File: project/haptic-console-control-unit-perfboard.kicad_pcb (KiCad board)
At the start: 2 copper layers, 90 x 144 mm, 239 parts, among them J1 JST-XH-5, J2 JST-XH-5

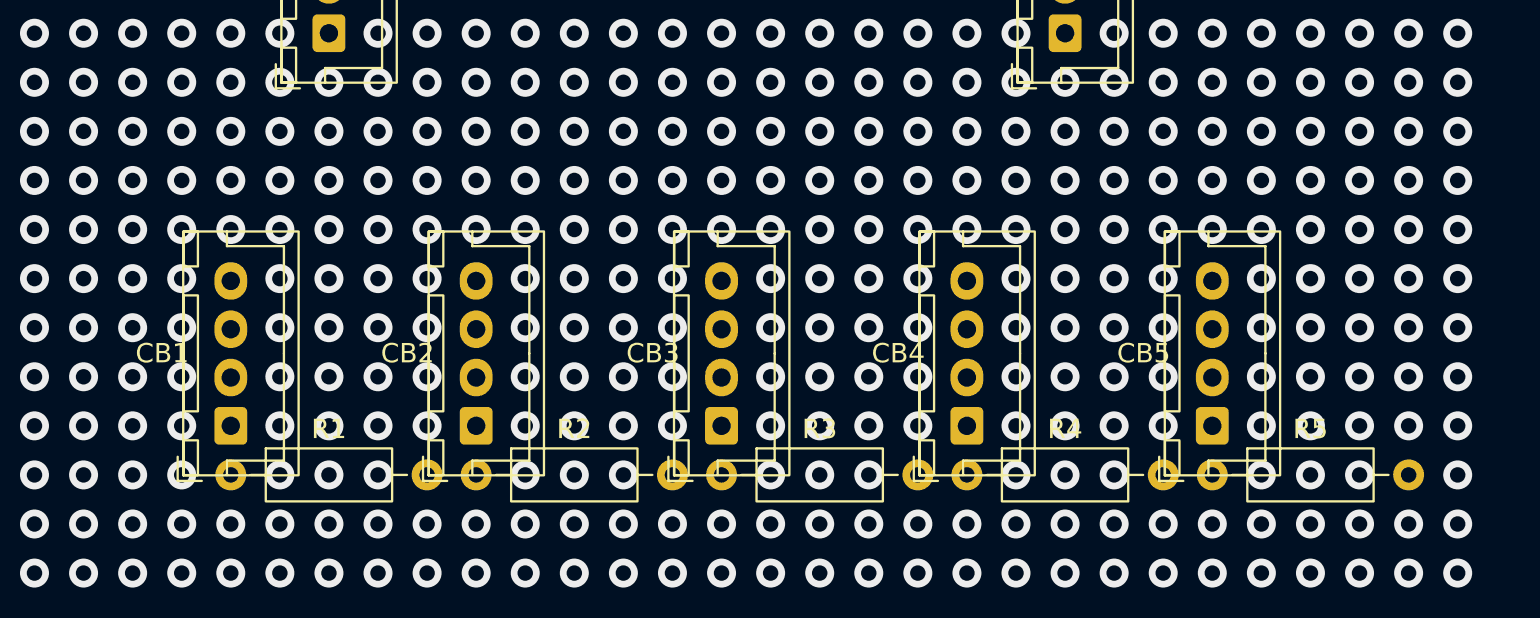
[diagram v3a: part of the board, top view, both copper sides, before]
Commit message: Resync every KiCad artifact to the current pin map (LED4 frozen on D13)
R4's LED jumper was re-landed from R29 (D16 = J1 pin 4, already soldered) to
O29 (D13), clearing the hardware conflict flagged last session. LED4 joins the
frozen set, which now holds 18 already-soldered conductors: B1-B8, J1/J2, LED4,
LED5. Freezing it costs nothing -- the solver had already chosen D13 -- so the
map stays at 1356.3 mm total Manhattan run, 61.0 mm longest wire.

- Schematic: 44 net labels renamed to their GPIO names (D<n>) via delete +
  re-add at identical coordinates. 2244 lines, 141 labels, ERC 0/0, 63 nets,
  all 40 signals verified on their intended U1 pin from the netlist libparts.
- Manufactured board: re-netted from a fresh netlist dump and re-routed via
  DSN -> Freerouting -> SES. 654 segments, 35 vias, DRC 0 violations /
  0 unconnected pads. Needed -mp 40; -mp 6 exited clean at 991.13 with one
  net still unrouted.
- Perfboard: R1-R5 moved upright beside their own CB in KiCad (they had only
  been patched into board_model.json before), 223 back-side jumper legs across
  6 tiers, 0 emit violations, 0 same-tier conflicts. Pristine DRC baseline is
  now 451 (was 478) -- moving the resistors off row 48 removed 27 violations --
  and the wired board's violation multiset is identical to it.
- Gerbers re-exported and re-zipped; all six renders regenerated, with zero
  wire overflow in all six colours confirmed by pixel measurement.
- Docs: wiring-guide.html regenerated (107 connections, 3006 mm, 157 pads /
  223 wires), panel-wiring-guide.html and README.md updated to match.

Co-Authored-By: Claude Opus 5 <noreply@anthropic.com>
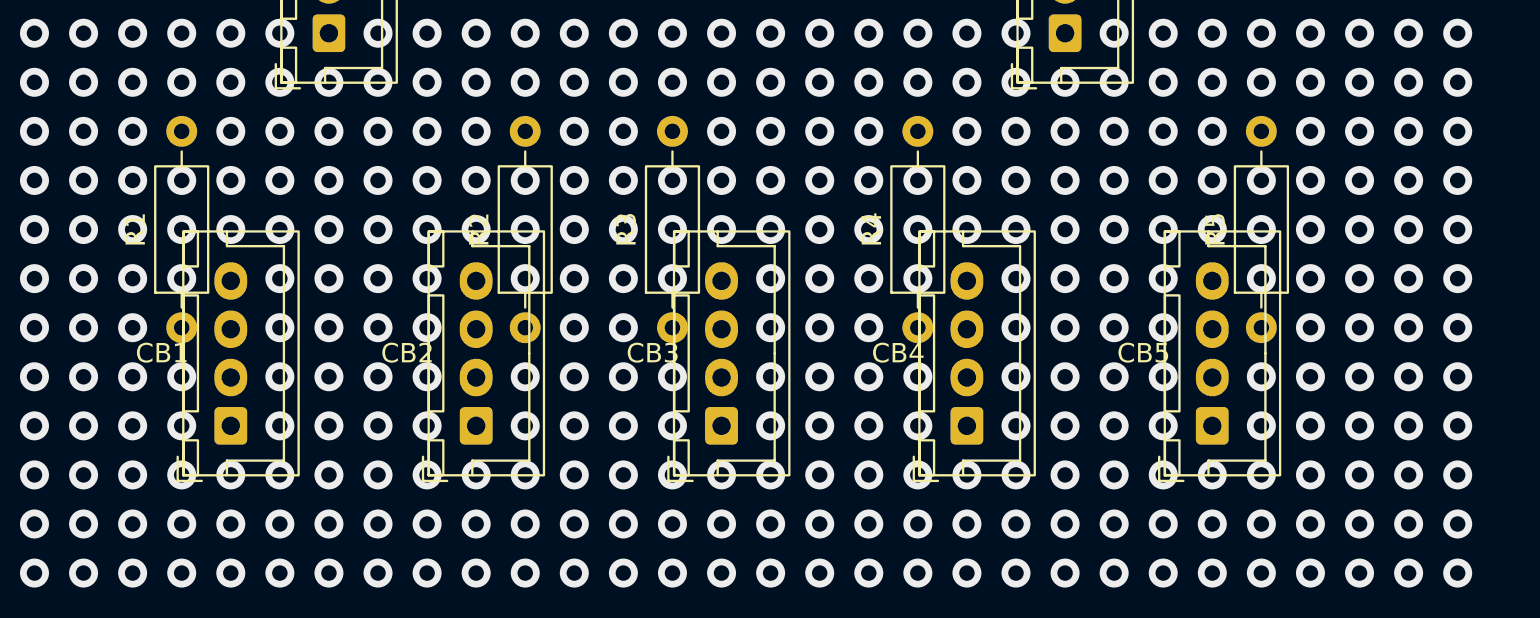
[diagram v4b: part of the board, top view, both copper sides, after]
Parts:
- added W204: D34 CB5.1->J_TEENSY_B.23, , B.Cu at (68.6, 92.8)
- added W205: D33 NP1.1->J_TEENSY_B.24, , B.Cu at (78.7, 94.0)
- added W206: D33 NP1.1->J_TEENSY_B.24, , B.Cu at (54.6, 111.8)
- added W207: D33 NP1.1->J_TEENSY_B.24, , B.Cu at (30.5, 71.2)
- added W208: D33 NP1.1->J_TEENSY_B.24, , B.Cu at (30.5, 108.0)
- added W209: D33 NP1.1->J_TEENSY_B.24, , B.Cu at (31.8, 104.1)
- added W210: D33 NP1.1->J_TEENSY_B.24, , B.Cu at (33.0, 88.9)
- added W211: D33 NP1.1->J_TEENSY_B.24, , B.Cu at (31.8, 73.7)
- added W212: D33 NP1.1->J_TEENSY_B.24, , B.Cu at (50.8, 68.7)
- added W213: D33 NP1.1->J_TEENSY_B.24, , B.Cu at (71.1, 71.2)
- added W214: LED_ARM CB1.3->R1.1, , B.Cu at (17.8, 114.3)
- added W215: LED_ARM CB1.3->R1.1, , B.Cu at (16.5, 114.3)
- added W216: LED_EN CB2.3->R2.1, , B.Cu at (30.5, 114.3)
- added W217: LED_EN CB2.3->R2.1, , B.Cu at (31.8, 114.3)
- added W218: LED_SFT CB3.3->R3.1, , B.Cu at (43.2, 114.3)
- added W219: LED_SFT CB3.3->R3.1, , B.Cu at (41.9, 114.3)
- added W220: LED_CONF CB4.3->R4.1, , B.Cu at (55.9, 114.3)
- added W221: LED_CONF CB4.3->R4.1, , B.Cu at (54.6, 114.3)
- added W222: LED_ALT CB5.3->R5.1, , B.Cu at (68.6, 114.3)
- added W223: LED_ALT CB5.3->R5.1, , B.Cu at (69.8, 114.3)
- W100, W101, W102: value D34 B5.2->J_TEENSY_A.23 -> D9 B8.2->J_TEENSY_A.11
- W103: value D34 B5.2->J_TEENSY_A.23 -> D26 B7.2->J_TEENSY_A.18
- W104, W105: value D13 NP1.5->J_TEENSY_A.14 -> D26 B7.2->J_TEENSY_A.18
- W106, W107: value D41 NP1.8->J_TEENSY_A.16 -> D26 B7.2->J_TEENSY_A.18
- W108, W109: value D40 NP1.7->J_TEENSY_A.17 -> D30 B6.2->J_TEENSY_A.22
- W110, W111: value D37 NP1.6->J_TEENSY_A.20 -> D30 B6.2->J_TEENSY_A.22
- W112: value D36 NP1.4->J_TEENSY_A.21 -> D30 B6.2->J_TEENSY_A.22
- W113, W114, W115: value D36 NP1.4->J_TEENSY_A.21 -> D32 B5.2->J_TEENSY_A.24
- W116, W117: value D30 NP1.3->J_TEENSY_B.22 -> D5 R1.2->J_TEENSY_A.7
- W118, W119: value D1 CB1.1->J_TEENSY_B.3 -> D5 R1.2->J_TEENSY_A.7
- W120: value D1 CB1.1->J_TEENSY_B.3 -> D6 CB2.1->J_TEENSY_A.8
- W121, W122: value D2 J1.1->J_TEENSY_B.4 -> D6 CB2.1->J_TEENSY_A.8
- W123, W124: value D3 J1.2->J_TEENSY_B.5 -> D6 CB2.1->J_TEENSY_A.8
- W125: value D3 J1.2->J_TEENSY_B.5 -> D10 NP1.4->J_TEENSY_A.12
- W126, W127: value D4 J1.3->J_TEENSY_B.6 -> D10 NP1.4->J_TEENSY_A.12
- W128, W129: value D4 J1.3->J_TEENSY_B.6 -> D11 NP1.8->J_TEENSY_A.13
- W130, W131: value D5 J1.4->J_TEENSY_B.7 -> D24 NP1.7->J_TEENSY_A.16
- W132: value D5 J1.4->J_TEENSY_B.7 -> D25 NP1.6->J_TEENSY_A.17
- W133: value D7 R1.2->J_TEENSY_B.9 -> D25 NP1.6->J_TEENSY_A.17
- W134, W135: value D7 R1.2->J_TEENSY_B.9 -> D28 NP1.5->J_TEENSY_A.20
- W136, W137: value D6 CB2.1->J_TEENSY_B.8 -> D28 NP1.5->J_TEENSY_A.20
- W138, W139, W140, W141: value D6 CB2.1->J_TEENSY_B.8 -> D29 R5.2->J_TEENSY_A.21
- W142, W143, W144: value D8 J2.1->J_TEENSY_B.10 -> D36 NP1.3->J_TEENSY_B.21
- W145, W146: value D9 J2.2->J_TEENSY_B.11 -> D36 NP1.3->J_TEENSY_B.21
- W147: value D9 J2.2->J_TEENSY_B.11 -> D23 CB1.1->J_TEENSY_B.4
- W148, W149, W150, W151: value D10 R2.2->J_TEENSY_B.12 -> D23 CB1.1->J_TEENSY_B.4
- W152, W153: value D11 CB3.1->J_TEENSY_B.13 -> D16 J1.4->J_TEENSY_B.11
- W154: value D11 CB3.1->J_TEENSY_B.13 -> D20 J1.3->J_TEENSY_B.7
- W155: value D12 R3.2->J_TEENSY_B.14 -> D20 J1.3->J_TEENSY_B.7
- W156, W157, W158: value D12 R3.2->J_TEENSY_B.14 -> D21 J1.2->J_TEENSY_B.6
- W159, W160: value D24 J2.3->J_TEENSY_B.16 -> D21 J1.2->J_TEENSY_B.6
- W161, W162, W163: value D25 J2.4->J_TEENSY_B.17 -> D22 J1.1->J_TEENSY_B.5
- W164: value D26 CB4.1->J_TEENSY_B.18 -> D22 J1.1->J_TEENSY_B.5
- W165, W166, W167: value D26 CB4.1->J_TEENSY_B.18 -> D17 R2.2->J_TEENSY_B.10
- W168, W169, W170: value D27 NP1.1->J_TEENSY_B.19 -> D17 R2.2->J_TEENSY_B.10
- W171: value D27 NP1.1->J_TEENSY_B.19 -> D15 R3.2->J_TEENSY_B.12
- W172, W173: value D28 R4.2->J_TEENSY_B.20 -> D15 R3.2->J_TEENSY_B.12
- W174, W175: value D28 R4.2->J_TEENSY_B.20 -> D14 CB3.1->J_TEENSY_B.13
- W176: value D29 NP1.2->J_TEENSY_B.21 -> D14 CB3.1->J_TEENSY_B.13
- W177, W178, W179: value D29 NP1.2->J_TEENSY_B.21 -> D13 R4.2->J_TEENSY_B.14
- W180, W181, W182: value D31 CB5.1->J_TEENSY_B.23 -> D41 J2.4->J_TEENSY_B.16
- W183, W184: value D32 R5.2->J_TEENSY_B.24 -> D40 J2.3->J_TEENSY_B.17
- W185: value D32 R5.2->J_TEENSY_B.24 -> D38 CB4.1->J_TEENSY_B.19
- W186: value LED_ARM CB1.3->R1.1 -> D38 CB4.1->J_TEENSY_B.19
- W187, W188: value LED_ARM CB1.3->R1.1 -> D39 J2.2->J_TEENSY_B.18
- W189, W190: value LED_EN CB2.3->R2.1 -> D39 J2.2->J_TEENSY_B.18
- W191, W192: value LED_EN CB2.3->R2.1 -> D37 J2.1->J_TEENSY_B.20
- W193, W194, W195: value LED_SFT CB3.3->R3.1 -> D37 J2.1->J_TEENSY_B.20
- W196: value LED_CONF CB4.3->R4.1 -> D37 J2.1->J_TEENSY_B.20
- W197, W198: value LED_CONF CB4.3->R4.1 -> D35 NP1.2->J_TEENSY_B.22
- W199, W200: value LED_ALT CB5.3->R5.1 -> D35 NP1.2->J_TEENSY_B.22
- W201, W202, W203: value LED_ALT CB5.3->R5.1 -> D34 CB5.1->J_TEENSY_B.23
- W22: value +3V3 S1.2->J_TEENSY_A.3 -> GND S1.1->B1.1
- W23, W24, W25, W26, W27: value +3V3 S1.2->J_TEENSY_A.3 -> +3V3 S1.2->S2.2
- W28, W29: value +3V3 S1.2->J_TEENSY_A.3 -> +5V S1.3->S2.3
- W30, W31: value +5V S1.3->J_TEENSY_A.1 -> +5V S1.3->S2.3
- W32: value +5V S1.3->J_TEENSY_A.1 -> SCL S1.5->S2.5
- W38, W39, W40: value SDA S1.4->S2.4 -> SCL S1.5->S2.5
- W43, W44, W45, W46: value IRQ1 S1.6->J_TEENSY_A.5 -> SDA S1.4->S2.4
- W47, W48, W49: value IRQ2 S2.6->J_TEENSY_A.4 -> SDA S1.4->S2.4
- W50, W51: value IRQ2 S2.6->J_TEENSY_A.4 -> IRQ1 S1.6->J_TEENSY_A.4
- W52, W53: value IRQ3 S3.6->J_TEENSY_A.10 -> IRQ1 S1.6->J_TEENSY_A.4
- W54, W55, W56, W57: value IRQ3 S3.6->J_TEENSY_A.10 -> IRQ2 S2.6->J_TEENSY_A.5
- W58, W59, W60: value IRQ4 S4.6->J_TEENSY_A.13 -> IRQ2 S2.6->J_TEENSY_A.5
- W61, W62, W63, W64, W65: value IRQ5 S5.6->J_TEENSY_A.19 -> IRQ3 S3.6->J_TEENSY_A.9
- W66, W67, W68, W69: value IRQ6 S6.6->J_TEENSY_A.24 -> IRQ3 S3.6->J_TEENSY_A.9
- W70, W71: value IRQ6 S6.6->J_TEENSY_A.24 -> IRQ4 S4.6->J_TEENSY_A.14
- W72, W73, W74: value D0 B1.2->J_TEENSY_B.2 -> IRQ4 S4.6->J_TEENSY_A.14
- W75, W76: value D0 B1.2->J_TEENSY_B.2 -> IRQ5 S5.6->J_TEENSY_A.19
- W77, W78, W79: value D21 B2.2->J_TEENSY_A.6 -> IRQ5 S5.6->J_TEENSY_A.19
- W80: value D21 B2.2->J_TEENSY_A.6 -> IRQ6 S6.6->J_TEENSY_A.23
- W81, W82, W83, W84: value D20 B3.2->J_TEENSY_A.7 -> IRQ6 S6.6->J_TEENSY_A.23
- W85, W86, W87, W88: value D16 B4.2->J_TEENSY_A.11 -> D0 B1.2->J_TEENSY_A.2
- W89, W90, W91: value D15 B8.2->J_TEENSY_A.12 -> D1 B2.2->J_TEENSY_A.3
- W92: value D39 B7.2->J_TEENSY_A.18 -> D1 B2.2->J_TEENSY_A.3
- W93, W94, W95: value D39 B7.2->J_TEENSY_A.18 -> D4 B3.2->J_TEENSY_A.6
- W96, W97, W98: value D35 B6.2->J_TEENSY_A.22 -> D8 B4.2->J_TEENSY_A.10
- W99: value D35 B6.2->J_TEENSY_A.22 -> D9 B8.2->J_TEENSY_A.11
- moved W31 86.3 mm to (11.4, 73.7)
- moved W10 85.4 mm to (7.62, 34.3)
- moved W9 85.1 mm to (43.2, 111.9)
- moved W6 78.4 mm to (41.9, 40.6)
- moved W47 73.0 mm to (76.2, 62.3)
- moved W134 70.8 mm to (80.0, 66.2)
- moved W136 69.7 mm to (71.1, 61.0)
- moved W58 68.7 mm to (11.4, 76.2)
- moved W1 64.8 mm to (17.8, 114.4)
- moved W133 63.6 mm to (53.3, 61.1)
- moved W80 62.8 mm to (71.1, 16.7)
- moved W39 62.2 mm to (19.1, 20.3)
- moved W75 61.0 mm to (58.4, 16.7)
- moved W59 60.2 mm to (21.6, 73.7)
- moved W116 59.5 mm to (22.9, 104.1)
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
